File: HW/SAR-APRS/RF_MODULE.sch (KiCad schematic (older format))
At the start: 19 parts

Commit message: schematic update
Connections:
- no-connect marks 7 -> 8
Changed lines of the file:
@@
 Text GLabel 7550 4550 2    50   Input ~ 0
 RFMOD_PTT
+NoConn ~ 6525 3550
 $EndSCHEMATC

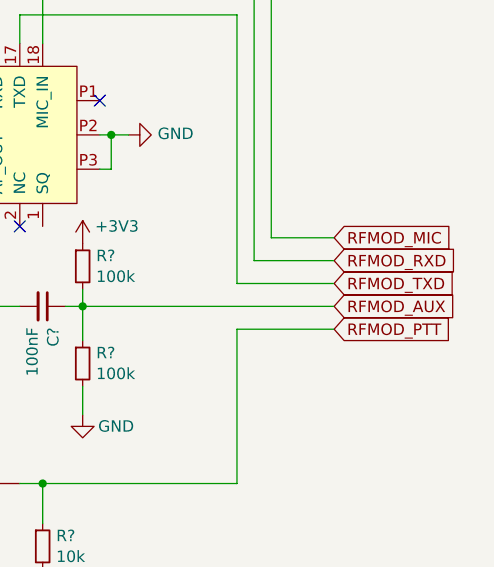
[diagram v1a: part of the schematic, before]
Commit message: schematic update
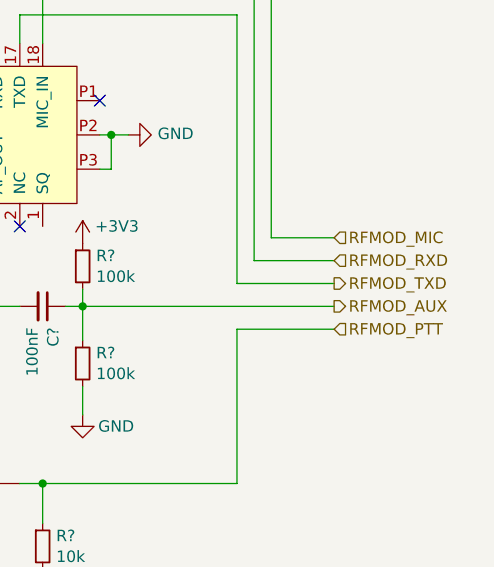
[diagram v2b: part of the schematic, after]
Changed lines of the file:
@@
 Wire Wire Line
 	7125 4550 7550 4550
-Text GLabel 7550 4150 2    50   Input ~ 0
-RFMOD_MIC
 Wire Wire Line
 	6450 4450 7550 4450
@@
 	6275 5225 7125 5225
 Connection ~ 6275 5225
-Text GLabel 7550 4250 2    50   Input ~ 0
+NoConn ~ 6525 3550
+Text HLabel 7550 4150 2    50   Input ~ 0
+RFMOD_MIC
+Text HLabel 7550 4250 2    50   Input ~ 0
 RFMOD_RXD
-Text GLabel 7550 4350 2    50   Input ~ 0
+Text HLabel 7550 4350 2    50   Output ~ 0
 RFMOD_TXD
-Text GLabel 7550 4450 2    50   Input ~ 0
+Text HLabel 7550 4450 2    50   Output ~ 0
 RFMOD_AUX
-Text GLabel 7550 4550 2    50   Input ~ 0
+Text HLabel 7550 4550 2    50   Input ~ 0
 RFMOD_PTT
-NoConn ~ 6525 3550
 $EndSCHEMATC

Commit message: schem and pcb update
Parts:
- C1, C2, C7: renamed from C?; footprint (none) -> Capacitors_SMD:C_0603
- C3, C4, C5, C6: renamed from C?; footprint (none) -> Capacitors_SMD:C_0805
- L1, L2, L3: renamed from L?; footprint (none) -> Inductors_SMD:L_0805
- R1, R2, R3, R4, R5: renamed from R?; footprint (none) -> Resistors_SMD:R_0603
- RV1: renamed from RV?; footprint (none) -> Potentiometers:Potentiometer_Trimmer-EVM3E
- gave numbers to parts that had none: 3

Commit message: PCB update
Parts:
- C1, C2, C7: footprint Capacitors_SMD:C_0603 -> Capacitors_SMD:C_0805
- J1: footprint w_conn_rf:coaxial_u.fl-r-smt-1 -> w_conn_rf:sma_straight_32k101-400l5
- R1, R2, R3, R4, R5: footprint Resistors_SMD:R_0603 -> Resistors_SMD:R_0805
- RV1: footprint Potentiometers:Potentiometer_Trimmer-EVM3E -> Potentiometers:Potentiometer_Trimmer_Bourns_3214J
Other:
- note added: "footprint ok"
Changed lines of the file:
@@
 F 0 "J1" H 3475 3150 50  0000 C CNN
 F 1 "uFl" H 3450 3025 50  0000 C CNN
-F 2 "w_conn_rf:coaxial_u.fl-r-smt-1" H 3425 2900 50  0001 C CNN
+F 2 "w_conn_rf:sma_straight_32k101-400l5" H 3425 2900 50  0001 C CNN
 F 3 " ~" H 3425 2900 50  0001 C CNN
 	1    3425 2900
@@
 F 0 "RV1" H 6525 2975 50  0000 R CNN
 F 1 "100k" H 6575 2875 50  0000 R CNN
-F 2 "Potentiometers:Potentiometer_Trimmer-EVM3E" H 6275 2725 50  0001 C CNN
+F 2 "Potentiometers:Potentiometer_Trimmer_Bourns_3214J" H 6275 2725 50  0001 C CNN
 F 3 "~" H 6275 2725 50  0001 C CNN
 	1    6275 2725
@@
 F 0 "C7" H 6367 4496 50  0000 L CNN
 F 1 "100nF" H 6367 4405 50  0000 L CNN
-F 2 "Capacitors_SMD:C_0603" H 6275 4450 50  0001 C CNN
+F 2 "Capacitors_SMD:C_0805" H 6275 4450 50  0001 C CNN
 F 3 "~" H 6275 4450 50  0001 C CNN
 	1    6275 4450
@@
 F 0 "R4" H 6509 4746 50  0000 L CNN
 F 1 "100k" H 6509 4655 50  0000 L CNN
-F 2 "Resistors_SMD:R_0603" H 6450 4700 50  0001 C CNN
+F 2 "Resistors_SMD:R_0805" H 6450 4700 50  0001 C CNN
 F 3 "~" H 6450 4700 50  0001 C CNN
 	1    6450 4700
@@
 F 0 "R3" H 6509 4321 50  0000 L CNN
 F 1 "100k" H 6509 4230 50  0000 L CNN
-F 2 "Resistors_SMD:R_0603" H 6450 4275 50  0001 C CNN
+F 2 "Resistors_SMD:R_0805" H 6450 4275 50  0001 C CNN
 F 3 "~" H 6450 4275 50  0001 C CNN
 	1    6450 4275
@@
 F 0 "R2" V 5350 4175 50  0000 C CNN
 F 1 "4k7" V 5600 4150 50  0000 C CNN
-F 2 "Resistors_SMD:R_0603" H 5425 4175 50  0001 C CNN
+F 2 "Resistors_SMD:R_0805" H 5425 4175 50  0001 C CNN
 F 3 "~" H 5425 4175 50  0001 C CNN
 	1    5425 4175
@@
 F 0 "R5" H 6334 5546 50  0000 L CNN
 F 1 "10k" H 6334 5455 50  0000 L CNN
-F 2 "Resistors_SMD:R_0603" H 6275 5500 50  0001 C CNN
+F 2 "Resistors_SMD:R_0805" H 6275 5500 50  0001 C CNN
 F 3 "~" H 6275 5500 50  0001 C CNN
 	1    6275 5500
@@
 F 0 "C1" H 6375 2400 50  0000 L CNN
 F 1 "100nF" H 6300 2300 50  0000 L CNN
-F 2 "Capacitors_SMD:C_0603" H 6600 2400 50  0001 C CNN
+F 2 "Capacitors_SMD:C_0805" H 6600 2400 50  0001 C CNN
 F 3 "~" H 6600 2400 50  0001 C CNN
 	1    6600 2400
@@
 F 0 "C2" H 7267 2771 50  0000 L CNN
 F 1 "10uF" H 7267 2680 50  0000 L CNN
-F 2 "Capacitors_SMD:C_0603" H 7175 2725 50  0001 C CNN
+F 2 "Capacitors_SMD:C_0805" H 7175 2725 50  0001 C CNN
 F 3 "~" H 7175 2725 50  0001 C CNN
 	1    7175 2725
@@
 F 0 "R1" V 6679 2725 50  0000 C CNN
 F 1 "620" V 6770 2725 50  0000 C CNN
-F 2 "Resistors_SMD:R_0603" H 6875 2725 50  0001 C CNN
+F 2 "Resistors_SMD:R_0805" H 6875 2725 50  0001 C CNN
 F 3 "~" H 6875 2725 50  0001 C CNN
 	1    6875 2725
@@
 Text HLabel 7550 4550 2    50   Input ~ 0
 RFMOD_PTT
+Text Notes 5200 2450 0    50   ~ 0
+footprint ok
 $EndSCHEMATC

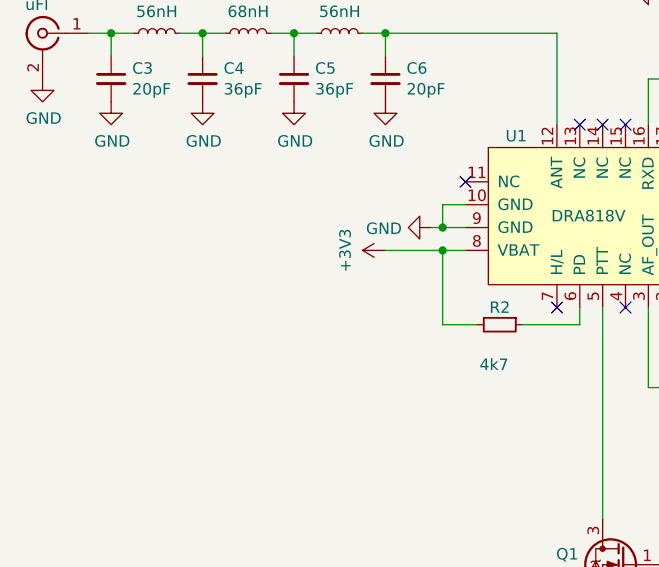
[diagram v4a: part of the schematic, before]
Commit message: DC-DC changed, PCB update
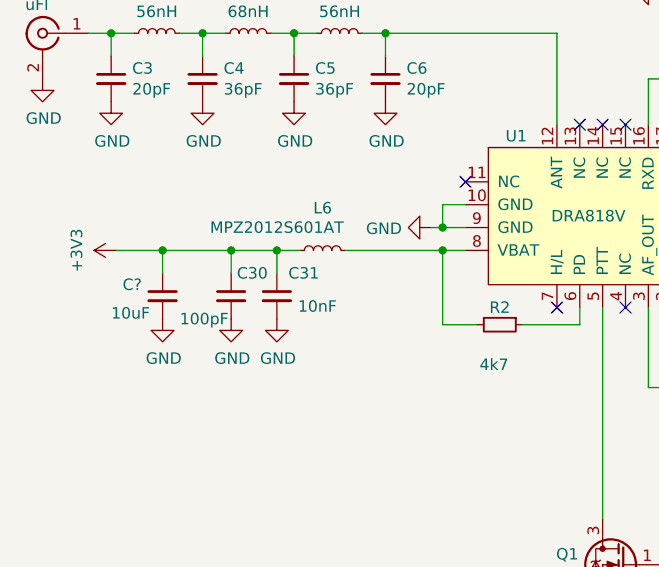
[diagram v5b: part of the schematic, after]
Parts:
- added C30: 100pF, Capacitors_SMD:C_0603, symbol device:C_Small
- added C31: 10nF, Capacitors_SMD:C_0603, symbol device:C_Small
- added C?: 10uF, Capacitors_SMD:C_1210, symbol device:C_Small
- added L6: MPZ2012S601AT, Capacitors_SMD:C_0805, symbol device:L_Small
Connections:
- net +3V3: now also C30.1, C31.1, C?.1, L6.1; no longer R2.2, U1.8 (VBAT)
- net GND: now also C30.2, C31.2, C?.2
- new net: L6.2, R2.2, U1.8 (VBAT)

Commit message: ibom added
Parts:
- gave numbers to parts that had none: 1
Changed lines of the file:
@@
 $EndComp
 $Comp
-L power:GND #PWR?
+L power:GND #PWR0177
 U 1 1 5E6A191B
 P 3950 4150
-F 0 "#PWR?" H 3950 3900 50  0001 C CNN
+F 0 "#PWR0177" H 3950 3900 50  0001 C CNN
 F 1 "GND" H 3955 3977 50  0000 C CNN
 F 2 "" H 3950 4150 50  0001 C CNN
@@
 AR Path="/5E6A484A" Ref="C?"  Part="1"
 AR Path="/5C97B601/5E6A484A" Ref="C?"  Part="1"
-AR Path="/5C8B81A5/5E6A484A" Ref="C?"  Part="1"
-F 0 "C?" H 3775 4100 50  0000 L CNN
+AR Path="/5C8B81A5/5E6A484A" Ref="C32"  Part="1"
+F 0 "C32" H 3775 4100 50  0000 L CNN
 F 1 "10uF" H 3725 3975 50  0000 L CNN
 F 2 "Capacitors_SMD:C_1210" H 3950 4050 50  0001 C CNN
